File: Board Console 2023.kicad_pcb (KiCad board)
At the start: 6 copper layers, 213.5 x 100.6 mm, 201 parts, among them J1 Raspberry PI, J10 I2C_Conn, J11 USB_C Power In, J13 SpeakerL, J14 SpeakerR, J15 Rasp_HDMI, J16 HDMI_OUT, J17 TTL 40Pin, J18 I2C EDID, J2 Composite OUT, J3 L1/L2, J4 Audio Jack OUT, J5 USB_B_Micro, J6 Comp_Display, J7 USB_A, J8 R1/R2, J9 V_BATT, SW10 A, SW11 X, SW12 Down, SW13 Left, SW14 Up, SW15 Right, SW16 Pow ON Button, SW17 SuperDX, SW3 Vol -, SW4 SuperSX, SW5 Select, SW6 Vol +, SW7 Start, SW8 B, SW9 Y, U1 MP3438GTL-P, U10 TS3DV642A0RUAR, U11 LM1117DT-3.3, U12 FAN5333BSX, U13 TFP401APZPR, U14 24LC02BT-E/LT, U15 LTC2950CTS8-1-TRMPBF, U2 MP3421GG-Z, U3 LM1117DT-3.3, U4 MP2722GRH-0000-P, U5 ADS1115IDGS, U6 NC7WV16P6X, U7 PAM8302AAD, U8 PAM8302AAD, U9 LM1117DT-3.3

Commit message: fix joypad area
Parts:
- H5: value MountingHole_Pad_MP -> GND
- H6: value MountingHole_Pad_MP -> +3.3V
- moved C7 12.1 mm to (69.9, 60.4)
- moved C11 12.1 mm to (79.1, 63.3)
- moved C16 12.1 mm to (78.1, 58.8)
- moved U7 12.1 mm to (74.2, 63.0)
- moved C13 12.1 mm to (78.3, 67.2)
- moved C8 12.1 mm to (70.3, 65.7)
- moved FB2 12.1 mm to (78.1, 60.5)
- moved FB3 12.1 mm to (78.1, 65.5)
- moved JP5 12.1 mm to (74.3, 59.7)
- moved R18 12.1 mm to (74.2, 65.7)
- moved R20 12.1 mm to (69.2, 62.2)
- moved R21 12.1 mm to (69.2, 64.0)
- moved RV1 12.1 mm to (74.3, 55.7)
- moved J3 7.85 mm to (77.1, 45.5), turned to -45 degrees
- moved J13 2.94 mm to (82.2, 56.8), turned to 0 degrees
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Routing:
- net /Audio Filter & Amplifier/OUT_L: track 71.9 -> 59.8 mm
- net Net-(C13-Pad1): track 226.7 -> 216.7 mm
- net /L2: track 63.6 -> 73.4 mm
- net SHTDWN: track 186.6 -> 178.2 mm
- net Net-(J13-Pin_2): track 13.5 -> 5.15 mm
- net /L1: track 63.8 -> 72.0 mm
- net /LEFT: track 47.8 -> 55.3 mm
- net /Composite OUT: track 208.4 -> 203.7 mm
- net SCL: track 48.6 -> 44.6 mm
- net /D+: track 132.4 -> 135.6 mm
- net SDA: track 49.4 -> 46.2 mm
- net RASP_3.3V: track 103.5 -> 106.6 mm
- net Net-(J13-Pin_1): track 195.9 -> 193.0 mm
- net /VBUS: track 138.3 -> 141.2 mm
- net Joy_Y: track 17.3 -> 20.1 mm
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- added copper zone on In4.Cu, net GND
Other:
- board size 213.5 x 100.6 mm -> 214.6 x 100.6 mm

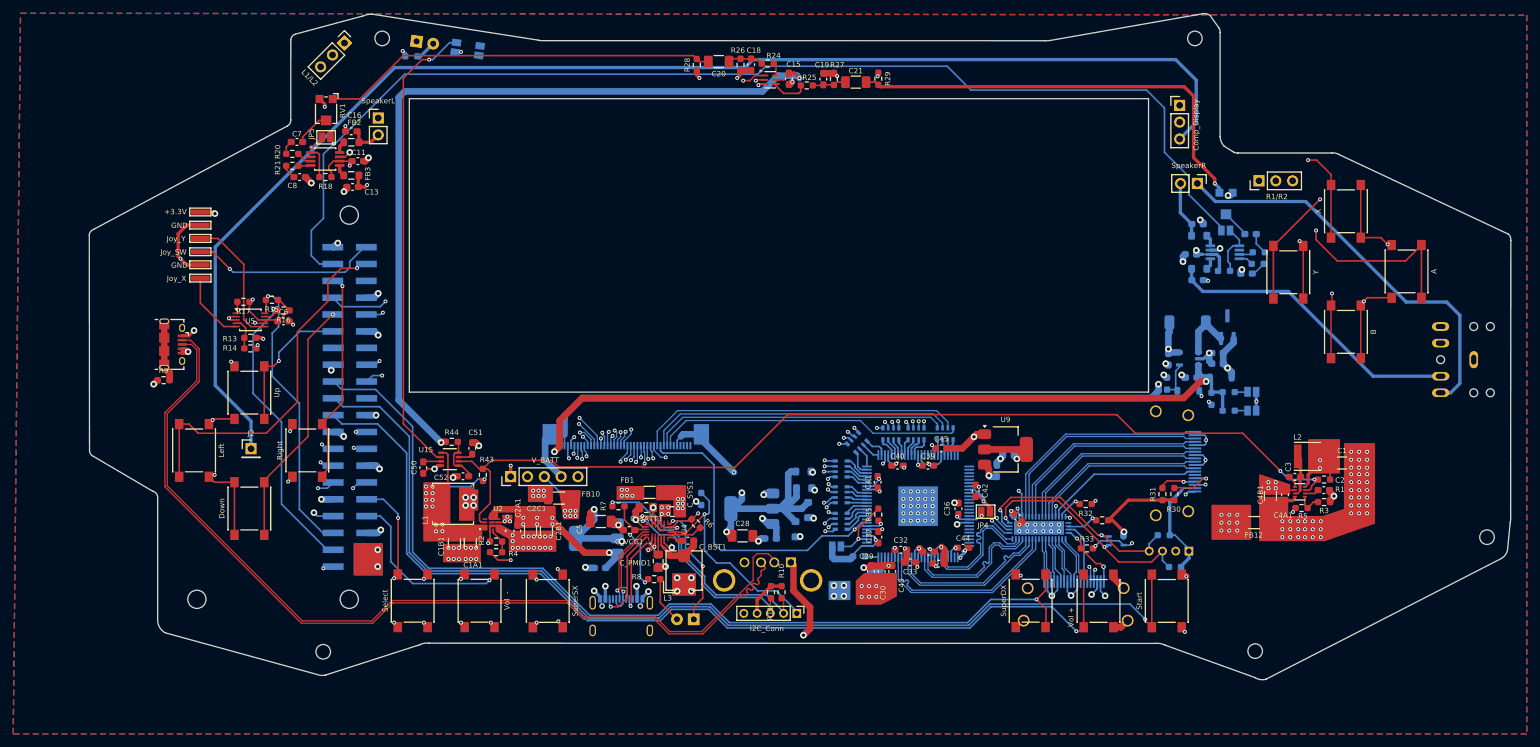
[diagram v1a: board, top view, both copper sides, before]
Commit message: fix hdmi traces and push button kill pin supply
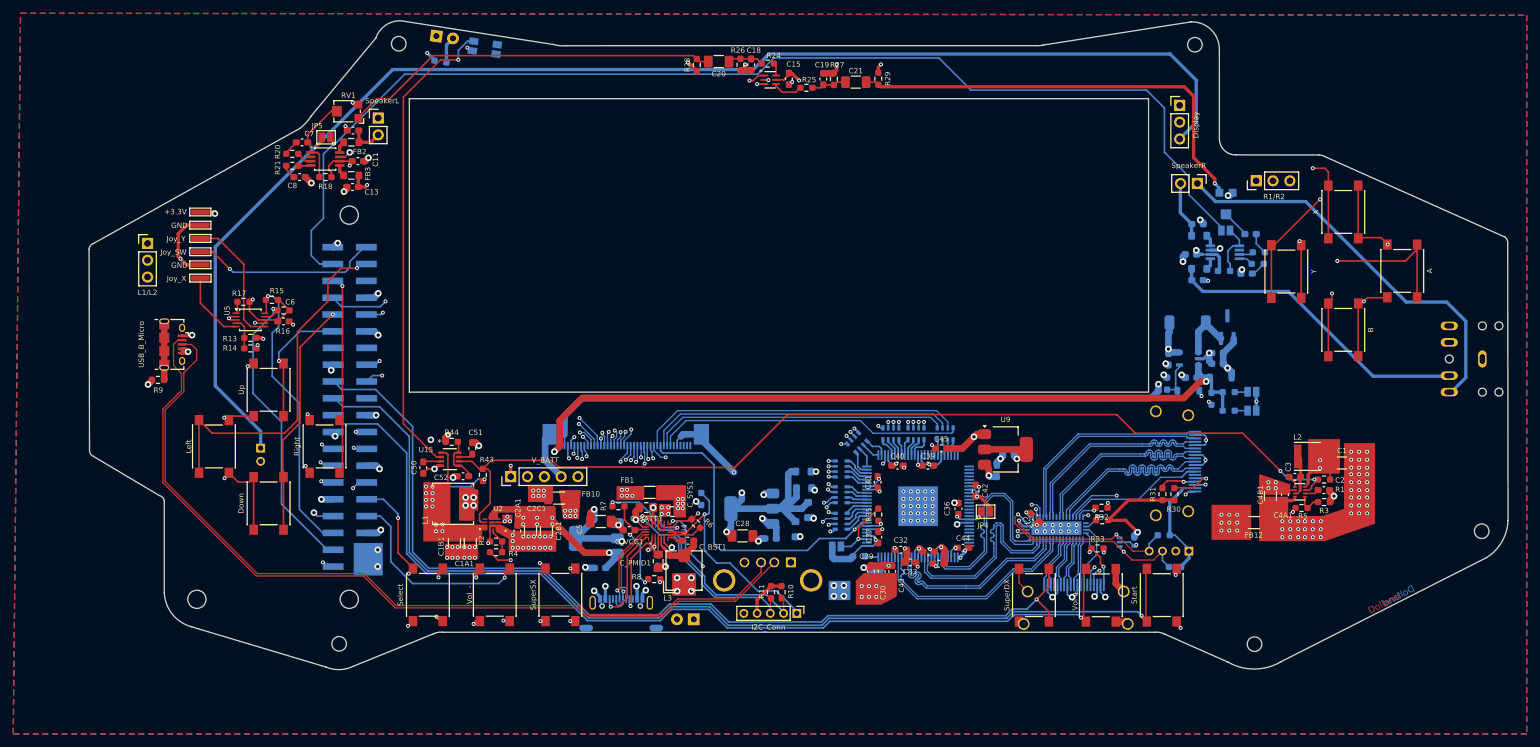
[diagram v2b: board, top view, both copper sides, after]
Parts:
- D1: value Charging LED -> CHG_LED
- J11: value USB_C Power In -> USB_C
- J2: footprint Connector_PinHeader_2.54mm:PinHeader_1x01_P2.54mm_Vertical -> Connector_PinHeader_2.00mm:PinHeader_1x02_P2.00mm_Vertical; moved to B.Cu
- J4: value Audio Jack OUT -> SJ1-3525N
- J6: value Comp_Display -> Display
- R6: value 2k -> 10k
- SW16: value Pow ON Button -> PWR_Push
- moved J3 42.4 mm to (47.4, 75.8), turned to 0 degrees
- moved R45 4.47 mm to (91.6, 48.3), turned to -9 degrees
- moved D5 3.09 mm to (91.0, 44.5)
- moved RV1 3.07 mm to (77.4, 55.8), turned to 180 degrees
- moved SW13 3.06 mm to (57.4, 106.4)
- moved SW12 3.00 mm to (65.7, 115.0)
- moved SW14 2.93 mm to (65.7, 97.8)
- moved H8 2.68 mm to (76.3, 136.2)
- moved SW15 2.67 mm to (74.1, 106.4)
- moved C24 2.64 mm to (181.4, 117.2)
- moved U10 2.64 mm to (184.6, 118.7)
- moved H11 2.62 mm to (85.3, 45.6)
- moved SW16 2.61 mm to (98.3, 46.2)
- moved SW3 2.47 mm to (99.8, 128.8)
- moved SW5 2.47 mm to (89.7, 128.8)
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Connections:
- net /HDMI Switch/CK+B renamed /HDMI Switch/CKB+
- net /HDMI Switch/CK-B renamed /HDMI Switch/CKB-
- net /HDMI Switch/D0+B renamed /HDMI Switch/D0B+
- net /HDMI Switch/D0-B renamed /HDMI Switch/D0B-
- net /HDMI Switch/D1+B renamed /HDMI Switch/D1B+
- net /HDMI Switch/D1-B renamed /HDMI Switch/D1B-
- net /HDMI Switch/D2+B renamed /HDMI Switch/D2B+
- net /HDMI Switch/D2-B renamed /HDMI Switch/D2B-
- net CK+A renamed CKA+
- net CK-A renamed CKA-
- net D0+A renamed D0A+
- net D0-A renamed D0A-
- net D1+A renamed D1A+
- net D1-A renamed D1A-
- net D2+A renamed D2A+
- net D2-A renamed D2A-
- J5 pad 1: /VBUS -> +5V
- J7 pad 1: /VBUS -> +5V
- R44 pad 1: +3.3V -> +5V
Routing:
- net /VBUS: track 141.2 -> 0.00 mm, vias 2 -> 0
- net /L2: track 73.4 -> 47.0 mm
- net /L1: track 72.0 -> 51.3 mm
- net D2A-: track 18.8 -> 31.4 mm
- net D2A+: track 18.6 -> 30.7 mm
- net RASP_3.3V: track 106.6 -> 95.0 mm
- net D1A+: track 21.0 -> 30.7 mm
- net D1A-: track 21.5 -> 30.7 mm
- net /D+: track 135.6 -> 126.8 mm
- net /D-: track 136.7 -> 128.2 mm
- net SDA_A: track 34.2 -> 27.8 mm
- net +5V: track 87.9 -> 93.3 mm, vias 19 -> 21
- net D0A-: track 24.9 -> 30.2 mm
- net D0A+: track 24.5 -> 29.0 mm
- net /HDMI Switch/SDA_B: track 25.2 -> 20.8 mm
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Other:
- board size 214.6 x 100.6 mm -> 214.2 x 98 mm
- board text added: "Comp"
- board text added: "Dolland"
- board text added: "GND"
